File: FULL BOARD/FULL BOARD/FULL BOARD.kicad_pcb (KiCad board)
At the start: 2 copper layers, 101 parts, among them IC1 TAS5760LDAP, J1 PJ-036AH-SMT-TR, J2 Micro_SD_Card, J3 B2B-PH-K-S, J4 5019514000, J5 61201021621, J6 B2B-PH-K-S, SW1 SW_Push, U1 LD1117S33TR_SOT223, U2 STM32H743VITx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

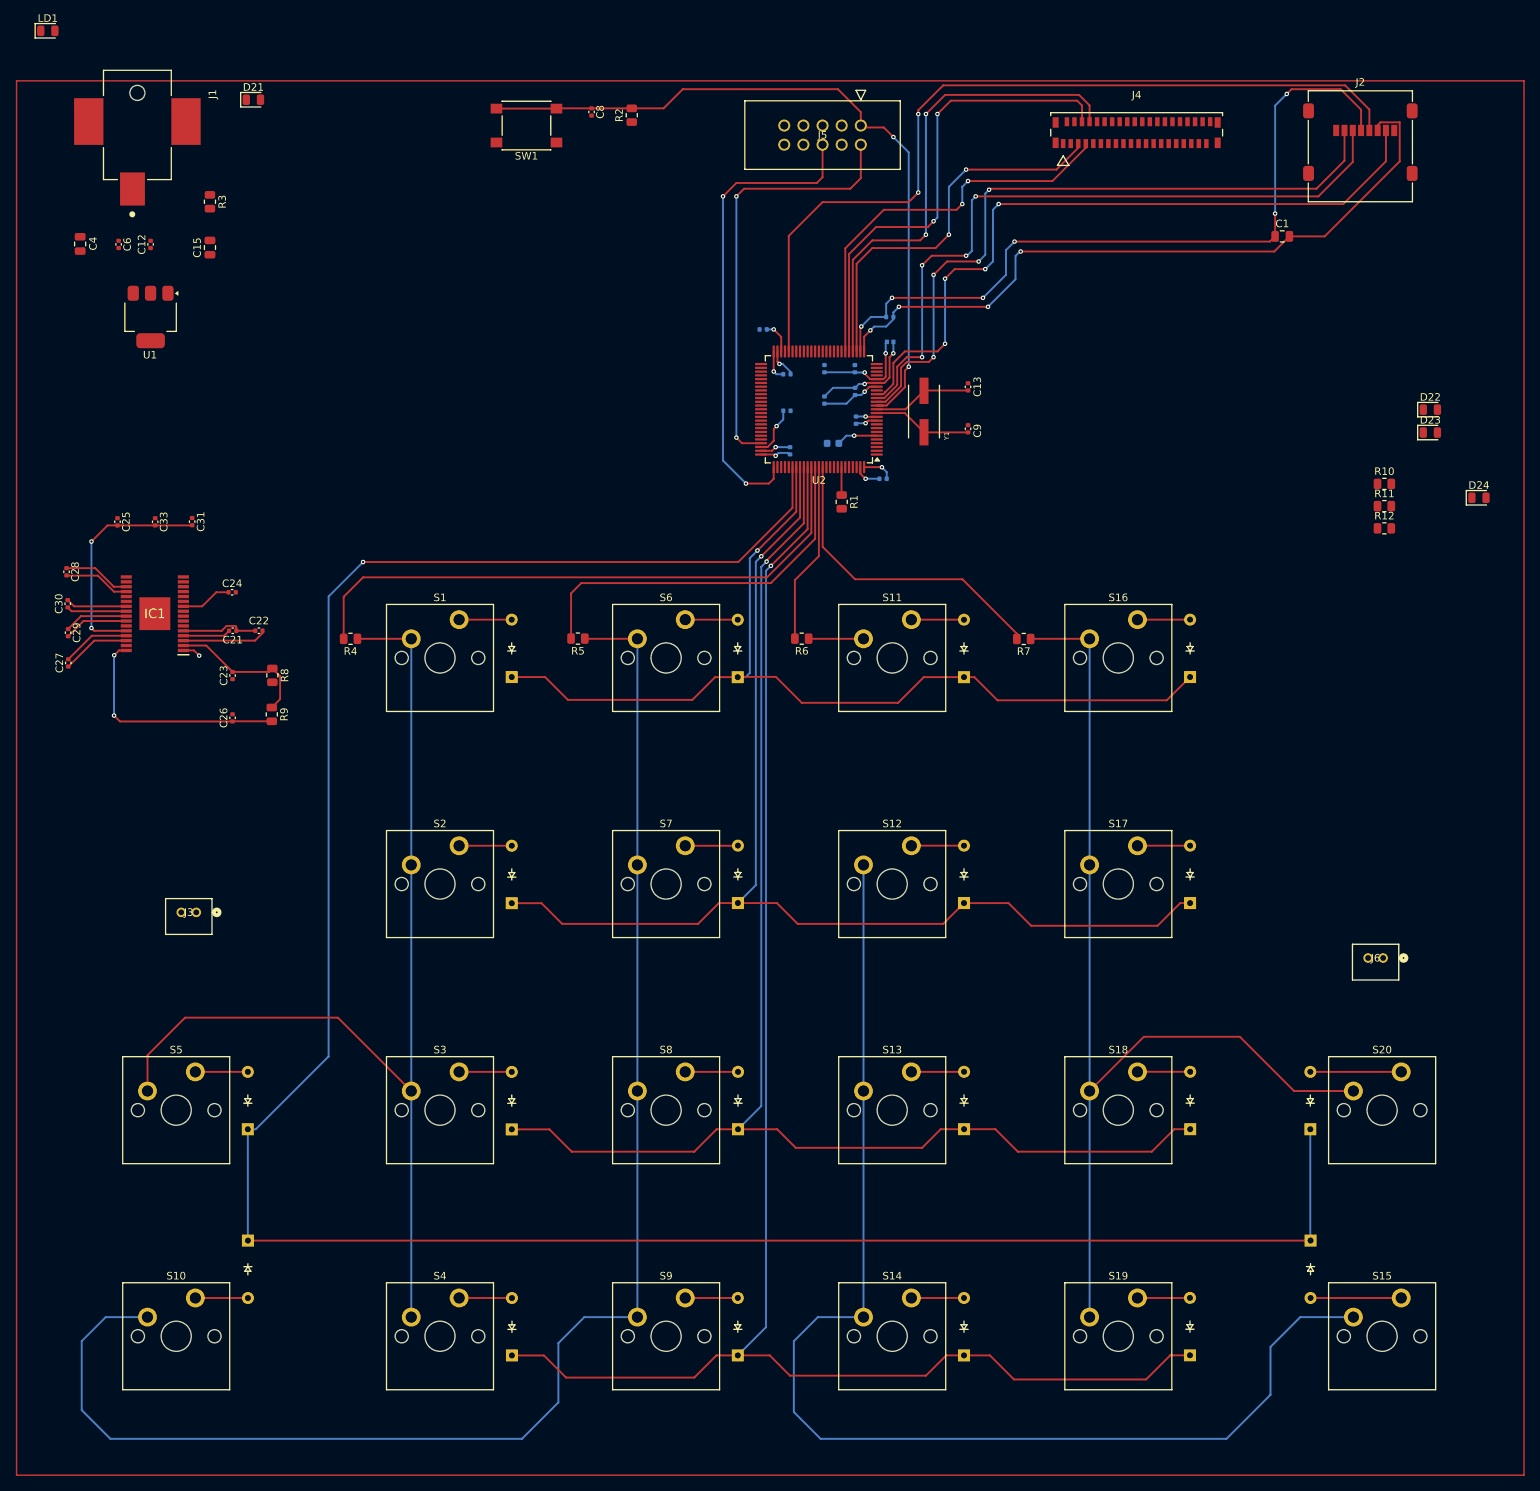
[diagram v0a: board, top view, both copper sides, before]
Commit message: power and audio routing added, needs to be checked
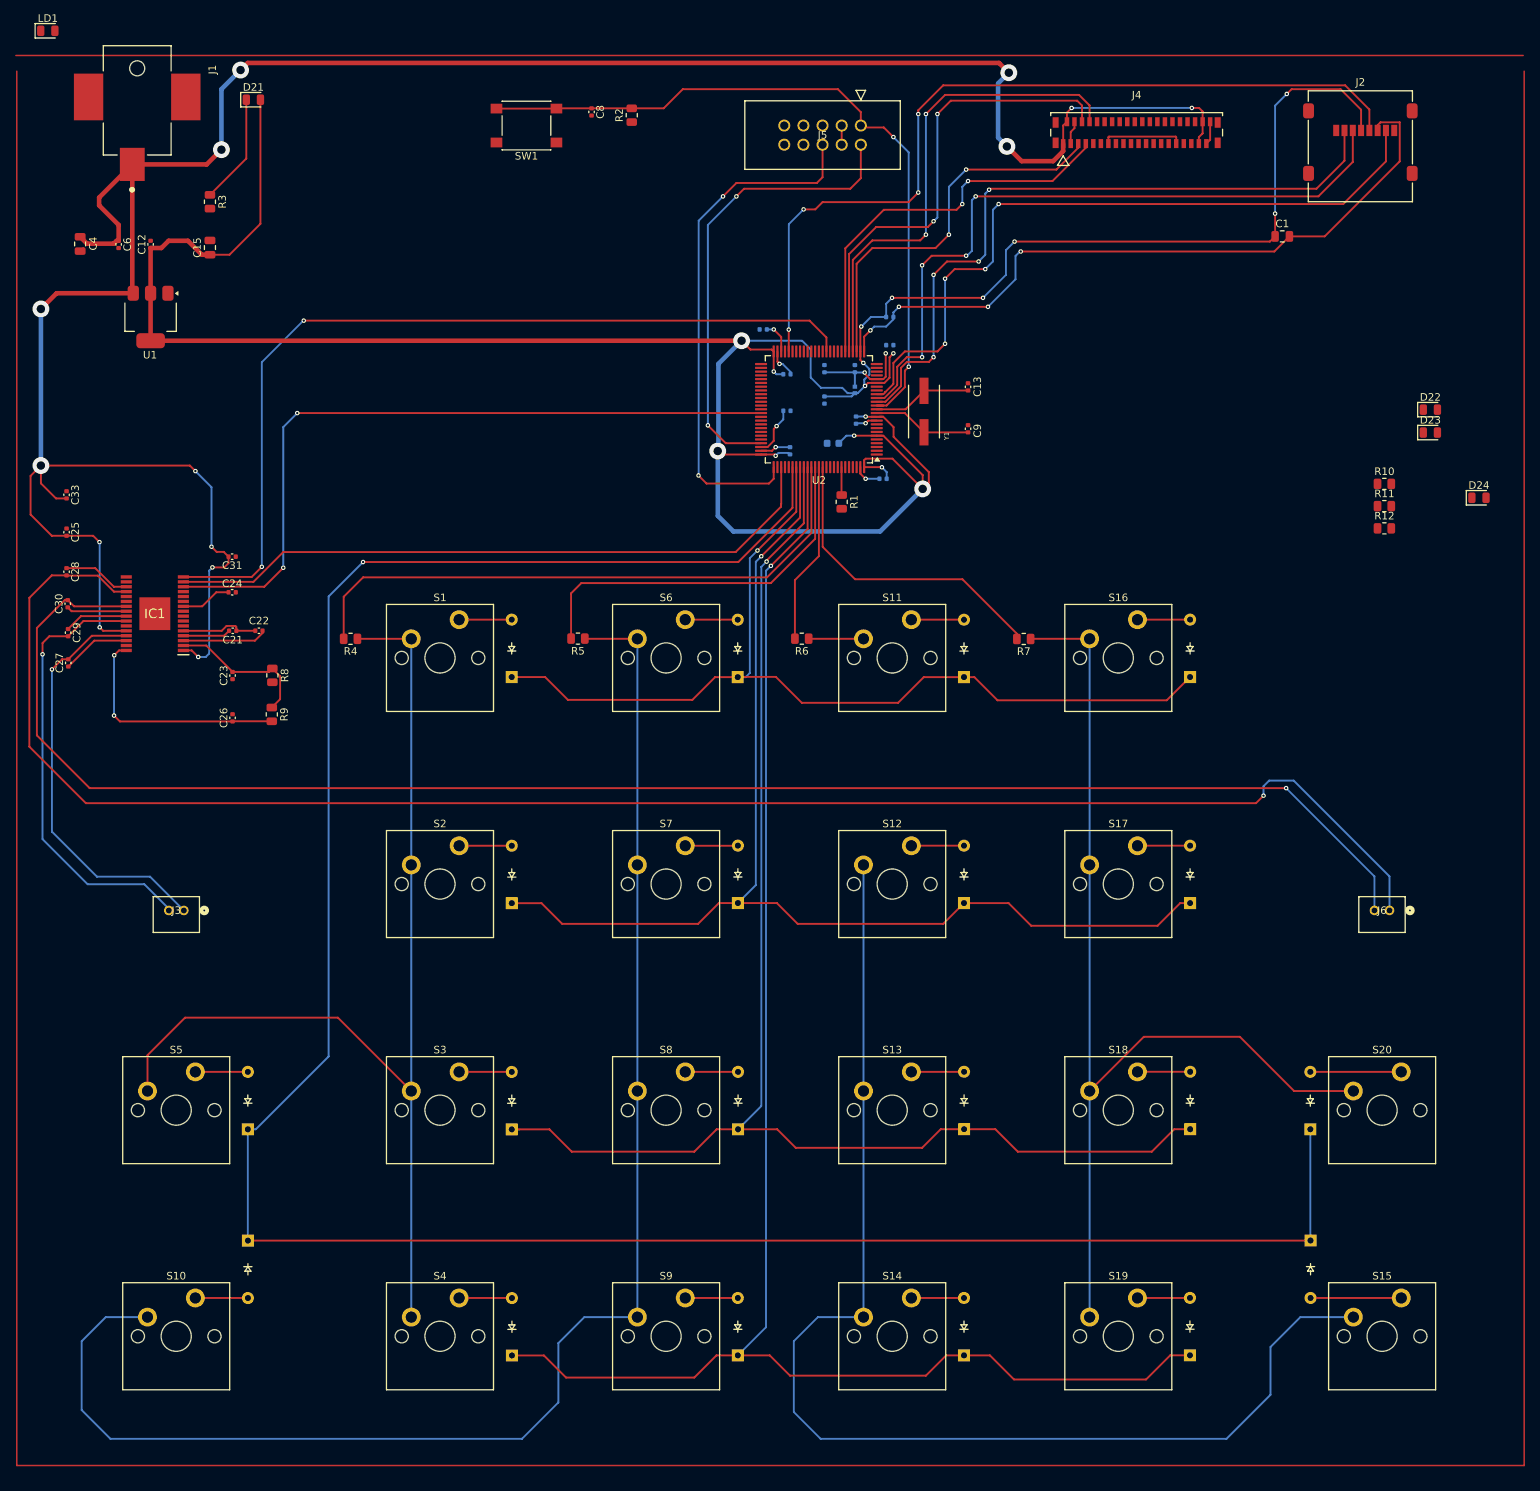
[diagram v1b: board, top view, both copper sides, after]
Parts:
- moved C33 12.3 mm to (26.2, 38.8)
- moved FL1 7.90 mm to (130.8, 24.9), turned to -90 degrees
- moved C20 7.68 mm to (135.4, 19.0), turned to 0 degrees
- moved C31 7.06 mm to (48.2, 47.0), turned to 180 degrees
- moved C25 6.89 mm to (26.2, 43.8)
- moved J6 6.37 mm to (201.7, 94.0)
- moved J1 3.26 mm to (34.9, -5.00)
- moved J3 1.67 mm to (41.8, 94.0)
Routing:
- net +5V: track 33.1 -> 337.5 mm, vias 3 -> 14
- net +3.3V: track 134.9 -> 382.7 mm, vias 13 -> 17
- net Net-(IC1-SPK_OUTB+): track 8.82 -> 230.1 mm, vias 0 -> 1
- net Net-(IC1-SPK_OUTB-): track 8.11 -> 217.7 mm, vias 0 -> 1
- net I2S_SD: track 0.00 -> 118.1 mm, vias 0 -> 2
- net I2S_MCLK: track 0.00 -> 97.1 mm, vias 0 -> 2
- net I2S_CK: track 0.00 -> 88.7 mm
- net Net-(IC1-SPK_OUTA-): track 8.56 -> 59.1 mm, vias 0 -> 1
- net Net-(IC1-SPK_OUTA+): track 8.99 -> 55.1 mm, vias 0 -> 1
- net Net-(D21-K): track 0.00 -> 14.6 mm
- net GND: track 117.0 -> 128.7 mm, vias 9 -> 8
- net /SWC: track 63.4 -> 69.2 mm
- net /SWDIO: track 57.5 -> 61.9 mm
- net /SD_CLK: track 111.1 -> 112.0 mm, vias 2 -> 4

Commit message: final(?) PCB before presentation
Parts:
- removed D22: LED, LED_SMD:LED_0805_2012Metric
- removed LD1: LED_Green, LED_SMD:LED_0805_2012Metric
- removed R12: 10k, Resistor_SMD:R_0805_2012Metric
- added D25: LED, LED_SMD:LED_0805_2012Metric, F.Cu at (211.0, 30.3)
- added R13: 10k, Resistor_SMD:R_0805_2012Metric, F.Cu at (203.1, 30.3)
- D1, D10, D11, D12, D13, D14, D15, D16, D17, D18, D19, D2, D20, D3, D4, D5, D6, D7, D8, D9: footprint Keyboard footprint:Diode_DO-35 -> ScottoKeebs_Components:Diode_DO-35
- FL1: footprint footprints:BEADC1005X55N -> Ferrite Bead:BEADC1005X55N
- IC1: footprint KiCad:SOP65P810X120-33N -> Audio Amp:DAP0032A_M
- J1: footprint PJ-036AH-SMT-TR:CUI_PJ-036AH-SMT-TR -> power jack:CONN3_PJ-036AH_CUD
- J3, J6: footprint audiojack:CONN2_B2B-PH-K-S_JST -> Audio Jack:CONN2_B2B-PH-K-S_JST
- J4: footprint footprints:CON_5019514000 -> Ribbon Connector:CON_5019514000
- J5: footprint footprints:CONN_61201021621_WRE -> Debugger:CONN_61201021621_WRE
- S1, S10, S11, S12, S13, S14, S15, S16, S17, S18, S19, S2, S20, S3, S4, S5, S6, S7, S8, S9: footprint Keyboard footprint:MX_PCB_1.00u -> ScottoKeebs_MX:MX_PCB_1.00u
- Y1: footprint footprints:XTAL_ABLS7M2-16.000MHZ-D-2Y-T -> crystal osc:XTAL_ABLS7M2_ABR
- moved C1 52.8 mm to (235.1, -18.4), turned to -90 degrees
- moved J1 42.9 mm to (65.4, -35.2), turned to 180 degrees
- moved D21 39.8 mm to (85.1, -34.1)
- moved J4 38.7 mm to (198.5, -33.2)
- moved J2 37.3 mm to (228.2, -29.1)
- moved J5 37.0 mm to (161.9, -31.5)
- moved SW1 36.4 mm to (117.4, -30.4)
- moved C8 36.3 mm to (125.9, -32.3)
- moved R2 36.3 mm to (131.3, -31.8)
- moved R3 34.5 mm to (75.4, -16.6)
- moved C15 34.4 mm to (75.4, -10.4)
- moved C4 34.4 mm to (58.2, -10.9)
- moved C12 34.4 mm to (67.6, -10.9)
- moved C6 34.4 mm to (63.3, -10.9)
- moved U1 34.4 mm to (67.6, -1.24)
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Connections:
- IC1 pad 33: unconnected-(IC1-EP-Pad33) -> +5V
- U2 pad 1: Net-(U2-PE2) -> unconnected-(U2-PE2-Pad1)
- U2 pad 96: unconnected-(U2-PB9-Pad96) -> Net-(U2-PB9)
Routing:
- net I2S_WS: track 51.7 -> 186.5 mm, vias 2 -> 4
- net GND: track 128.7 -> 245.0 mm, vias 8 -> 11
- net +3.3V: track 382.7 -> 485.4 mm, vias 17 -> 20
- net Net-(U2-PE1): track 0.00 -> 51.7 mm
- net Net-(U2-PE0): track 0.00 -> 49.7 mm
- net Net-(U2-PB9): track 0.00 -> 48.7 mm
- net +5V: track 337.5 -> 378.2 mm
- net Net-(R6-Pad1): track 173.4 -> 201.9 mm
- net /LCD_MOSI: track 53.0 -> 73.9 mm
- net /SD_DO: track 95.2 -> 111.3 mm
- net /SWC: track 69.2 -> 85.0 mm
- net /SD_DI: track 92.8 -> 107.9 mm
- net /SD_CLK: track 112.0 -> 126.8 mm
- net /SWDIO: track 61.9 -> 76.4 mm
- net /LCD_SCK: track 64.7 -> 78.7 mm
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- added copper zone on B.Cu, net GND
- added copper zone on F.Cu, net GND
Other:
- board outline added: 200 x 200 mm

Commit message: Gerber added, 3D CAD added
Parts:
- D1, D10, D11, D12, D13, D14, D15, D16, D17, D18, D19, D2, D20, D3, D4, D5, D6, D7, D8, D9: moved to B.Cu
- J4: footprint Ribbon Connector:CON_5019514000 -> real ribbon:CON_5051104091_MOL
- moved Y1 87.0 mm to (192.7, 106.8)
- moved C9 86.8 mm to (189.1, 110.3), turned to -90 degrees
- moved C11 86.8 mm to (182.5, 115.7)
- moved C12 86.8 mm to (85.2, 74.1)
- moved C14 86.8 mm to (170.2, 112.0)
- moved C15 86.8 mm to (93.1, 74.5)
- moved C16 86.8 mm to (169.8, 101.8)
- moved C2 86.8 mm to (166.6, 95.9)
- moved C21 86.8 mm to (96.3, 135.9)
- moved C22 86.8 mm to (99.7, 135.9)
- moved C23 86.8 mm to (96.2, 141.8)
- moved C24 86.8 mm to (96.2, 130.8)
- moved C25 86.8 mm to (74.2, 122.8)
- moved C27 86.8 mm to (74.4, 140.1)
- moved C3 86.8 mm to (175.9, 111.0)
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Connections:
- J4 pad 5: I2S_WS -> /LCD_CS
- U2 pad 15: /SD_CS -> unconnected-(U2-PC0-Pad15)
- U2 pad 28: I2S_WS -> /LCD_CS
- U2 pad 51: unconnected-(U2-PB12-Pad51) -> /SD_CS
- U2 pad 77: unconnected-(U2-PA15-Pad77) -> I2S_WS
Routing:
- net I2S_WS: track 186.5 -> 94.9 mm, vias 4 -> 0
- net /LCD_CS: track 0.00 -> 76.7 mm, vias 0 -> 2
- net /SD_CS: track 105.5 -> 140.4 mm, vias 4 -> 2
- net GND: track 245.0 -> 266.7 mm, vias 11 -> 12
- net /LCD_MOSI: track 73.9 -> 77.8 mm
- net /HSE_IN: track 15.4 -> 12.2 mm
- net /HSE_OUT: track 15.3 -> 12.1 mm
- net +5V: track 378.2 -> 380.8 mm
- net /SD_CLK: track 126.8 -> 128.3 mm
- net /SD_DI: track 107.9 -> 106.8 mm
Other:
- outline, holes or cut-outs redrawn
- board text added: "Conundrum Crack"
